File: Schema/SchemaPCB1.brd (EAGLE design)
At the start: 48.9 x 100 mm, 25 parts, among them J1 CON-HIROSE-COAXIAL-U.FL, J2 Programmer, U1 RN2483, U2 TPS22860DBVR, U3 ESP32, U4 SOT-89-5, U5 SI7217-B-01-IVR

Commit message: pull-up toegevoegd op I2C gps
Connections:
- net N$8 renamed VCC
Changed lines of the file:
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@@
 <wire x1="2.8956" y1="-4.699" x2="12.21" y2="51.435" width="0" layer="19" extent="1-1"/>
-</signal>
-<signal name="N$8">
-<contactref element="U?1" pad="VCC"/>
-<contactref element="L1" pad="1"/>
-<wire x1="11.35" y1="-8.85" x2="1.255" y2="-20.32" width="0" layer="19" extent="1-1"/>
 </signal>
 <signal name="N$6">
@@
 <wire x1="0.9652" y1="-4.699" x2="2.555" y2="-20.32" width="0" layer="19" extent="1-1"/>
 </signal>
+<signal name="VCC">
+<contactref element="U?1" pad="VCC"/>
+<contactref element="L1" pad="1"/>
+<wire x1="11.35" y1="-8.85" x2="1.255" y2="-20.32" width="0" layer="19" extent="1-1"/>
+</signal>
 </signals>

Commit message: gps schema aangepast
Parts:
- T1: value (none) -> SiSH615ADN
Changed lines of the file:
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@@
 <attribute name="NAME" x="19.05" y="33.02" size="1.27" layer="25" align="center"/>
 </element>
-<element name="T1" library="zetex" library_urn="urn:adsk.eagle:library:418" package="SOT-23" package3d_urn="urn:adsk.eagle:package:30981/1" value="" x="1.905" y="-5.715" smashed="yes">
+<element name="T1" library="zetex" library_urn="urn:adsk.eagle:library:418" package="SOT-23" package3d_urn="urn:adsk.eagle:package:30981/1" value="SiSH615ADN" x="1.905" y="-5.715" smashed="yes">
 <attribute name="MF" value="" x="1.905" y="-5.715" size="1.778" layer="27" display="off"/>
 <attribute name="MPN" value="" x="1.905" y="-5.715" size="1.778" layer="27" display="off"/>

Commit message: Bezig aan board
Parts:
- removed R2, R3: 4k6Û, --CoolTeamLib:M0805
- added C10, C12: (no value), rcl:C0805
- added R4, R5, R6, R7, R8: (no value), rcl:R0805
- moved L1 112.6 mm to (-4.45, 92.1)
- moved U?1 95.3 mm to (6.99, 82.5)
- moved T1 77.5 mm to (1.91, 71.8)
- moved C7 40.1 mm to (42.5, 87.6)
- moved U2 33.0 mm to (38.7, 87.6), turned to 90 degrees
- moved C6 26.3 mm to (36.2, 82.5), turned to 270 degrees
- moved U5 18.7 mm to (23.5, 12.1)
- moved J3 13.4 mm to (1.91, 58.4)
- moved J1 3.81 mm to (26.7, 97.8)
- moved U1 3.81 mm to (16.5, 67.9)
- moved U4 3.24 mm to (44.5, 83.2)
- moved C4 3.18 mm to (42.5, 78.7)
- moved C5 2.54 mm to (46.4, 78.7)
- moved C3 1.91 mm to (43.2, 71.8)
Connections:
- removed net VCC: L1.1, U?1.VCC
- new net GPS_ENABLE: R8.1
- new net N$8: C10.1, C12.1, L1.1, R5.2, U?1.VCC
- net *GPS_ENABLE: now also R8.2
- net +3V3: now also R6.2, R7.2; no longer R2.2, R3.2
- net GND: now also C10.2, C12.2, R4.2
- net I2C_SCL: now also R6.1; no longer R2.1
- net I2C_SDA: now also R7.1; no longer R3.1
- net N$5: now also R4.1
- net N$6: now also R5.1
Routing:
- net RN2483_RESET: track 0.00 -> 44.6 mm
- net RN2483_ENABLE: track 39.1 -> 0.00 mm
- net GND: track 92.7 -> 68.0 mm
- net I2C_SCL: track 21.4 -> 0.00 mm
- net I2C_SDA: track 14.2 -> 0.00 mm
- net +3V3: track 97.0 -> 99.8 mm
- net RN2483_VDD: track 25.4 -> 23.1 mm
- net BAT_IN: track 4.59 -> 3.09 mm
- net TXD2: track 47.7 -> 46.6 mm

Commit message: Eagle fix
Board bijna klaar
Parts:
- removed R4, R5, R8: (no value), rcl:R0805
- removed T1: SiSH615ADN, zetex:SOT-23
- added C11, C13: (no value), rcl:C0805
- added U6: TPS22860DBVR, --CoolTeamLib:SOT95P280X145-6N
- moved U5 20.3 mm to (22.9, 32.4)
- moved C10 17.1 mm to (10.2, 82.5)
- moved C12 16.9 mm to (10.2, 80.6)
- moved L1 16.5 mm to (10.2, 84.5), turned to 180 degrees
- moved R7 12.8 mm to (8.26, 38.1), turned to 270 degrees
- moved U?1 8.25 mm to (6.99, 74.3)
- moved R6 3.24 mm to (5.08, 38.1)
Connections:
- removed net *GPS_ENABLE: R8.2, T1.3, U3.32
- removed net N$1: U3.38, U3.39, U3.40, U3.41, U3.42, U3.43, U3.44, U3.45, U3.46, U3.47
- removed net N$2: J3.1
- removed net N$3: J3.2
- removed net N$5: R4.1, U?1.WAKE-UP
- removed net N$8: C10.1, C12.1, L1.1, R5.2, U?1.VCC
- new net IO1: J3.3, U3.22
- new net IO2: J3.2, U3.23
- new net IO3: J3.1, U3.24
- net +3V3: now also C13.1, U6.4, U6.5; no longer T1.1
- net GND: now also C11.2, C13.2, U3.38, U3.39, U3.40, U3.41, U3.42, U3.43, U3.44, U3.45, U3.46, U3.47, U6.2, U?1.WAKE-UP; no longer R4.2
- net GPS_ENABLE: now also U3.32, U6.6; no longer R8.1
- net HALL_DATA: no longer J3.3
- net N$6: now also C10.1, C12.1, L1.1, U?1.VCC; no longer R5.1
- net N$7: now also C11.1, U6.1; no longer T1.2
- net RXD0: now also J3.5; no longer J3.6
- net TXD0: now also J3.6; no longer J3.5
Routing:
- net GND: track 68.0 -> 325.0 mm, vias 0 -> 12
- net +3V3: track 99.8 -> 240.2 mm, vias 0 -> 2
- net I2C_SDA: track 0.00 -> 95.9 mm, vias 0 -> 2
- net I2C_SCL: track 0.00 -> 76.6 mm, vias 0 -> 2
- net RN2483_ENABLE: track 0.00 -> 70.3 mm, vias 0 -> 2
- net GPS_ENABLE: track 0.00 -> 49.7 mm, vias 0 -> 2
- net RXD0: track 0.00 -> 49.4 mm, vias 0 -> 2
- net HALL_EN: track 0.00 -> 49.0 mm, vias 0 -> 1
- net TXD0: track 0.00 -> 47.7 mm, vias 0 -> 2
- net IO1: track 0.00 -> 22.1 mm, vias 0 -> 1
- net IO2: track 0.00 -> 18.7 mm, vias 0 -> 1
- net N$6: track 0.00 -> 18.2 mm
- net HALL_DATA: track 0.00 -> 17.5 mm
- net IO3: track 0.00 -> 16.0 mm, vias 0 -> 1
- net N$7: track 0.00 -> 7.70 mm
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- added copper zone on layer 1, net GND
- added copper zone on layer 16, net GND
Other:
- board size 48.9 x 100 mm -> 48.9 x 71.4 mm
- board text added: "3V3"
- board text added: "C:/Users/nielv/Pictures/sincere_partners_KU-Leuven (2).bmp"
- board text added: "E_EN"
- board text added: "GND"
- board text added: "H_EN"
- board text added: "I/O"
- board text added: "PCB design: niel_v"
- board text added: "RXD0"
- board text added: "SCL"
- board text added: "SDA"
- board text added: "TXD0"

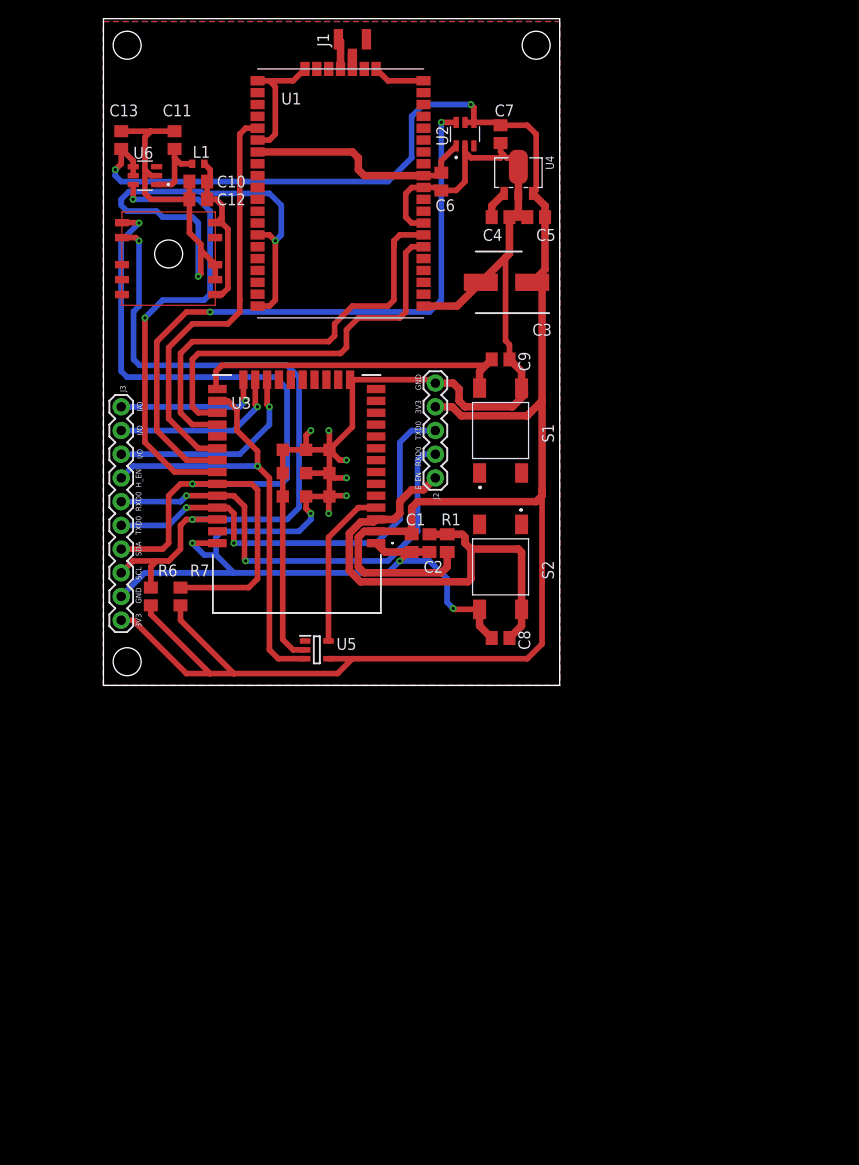
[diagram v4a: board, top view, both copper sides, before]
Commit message: laatste componenten en pcb2 toegevoegd
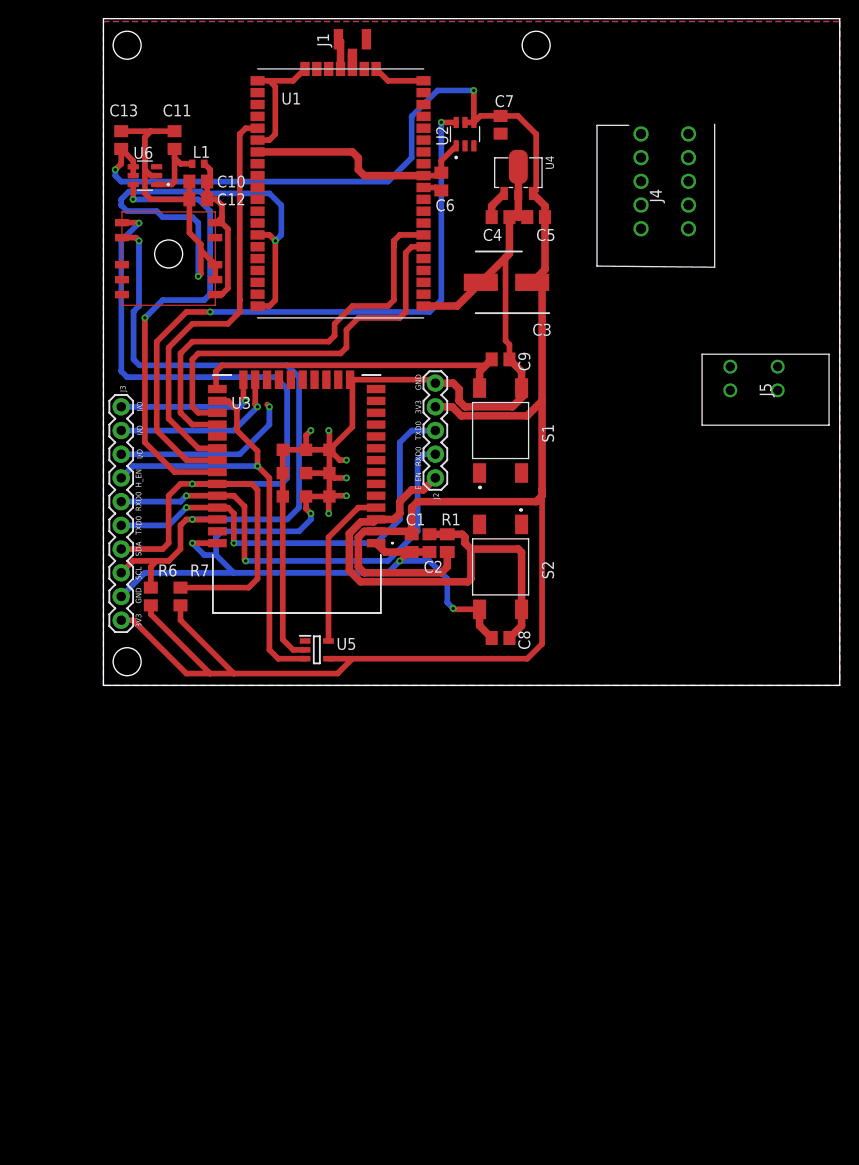
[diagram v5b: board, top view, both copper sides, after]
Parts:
- added J4: 39700-0205, --CoolTeamLib:397000205
- added J5: 39700-0002, --CoolTeamLib:397000002
- moved C7 1.00 mm to (42.5, 88.6)
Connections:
- new net HDC2010_INT: J4.10, J4.9, U3.10
- net +3V3: now also J4.1, J4.2
- net BAT_IN: now also J5.2, J5.4
- net GND: now also J4.3, J4.4, J5.1, J5.3
- net I2C_SCL: now also J4.7, J4.8
- net I2C_SDA: now also J4.5, J4.6
- net IO1: now also U3.13; no longer U3.22
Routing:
- net GND: track 325.0 -> 303.7 mm
- net +3V3: track 240.2 -> 243.1 mm
- net IO1: track 22.1 -> 19.4 mm
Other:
- board size 48.9 x 71.4 mm -> 78.9 x 71.4 mm

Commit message: BOARD klaar
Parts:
- moved J4 41.1 mm to (59.7, 36.5)
- moved J5 14.4 mm to (56.3, 72.2), turned to 0 degrees
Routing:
- net GND: track 303.7 -> 409.7 mm, vias 12 -> 13
- net I2C_SCL: track 76.6 -> 140.5 mm, vias 2 -> 3
- net I2C_SDA: track 95.9 -> 154.3 mm, vias 2 -> 3
- net HDC2010_INT: track 0.00 -> 52.0 mm, vias 0 -> 2
- net +3V3: track 243.1 -> 287.7 mm
- net BAT_IN: track 3.09 -> 26.6 mm, vias 0 -> 1
- net IO1: track 19.4 -> 29.7 mm
- net RN2483_ENABLE: track 70.3 -> 73.4 mm
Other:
- board size 78.9 x 71.4 mm -> 63.9 x 71.4 mm
